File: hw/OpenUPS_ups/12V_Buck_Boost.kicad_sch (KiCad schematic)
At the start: 61 parts, among them Q601 AON7534, Q602 AON7534, Q603 AON7534, Q604 AON7534, U601 NCP81599

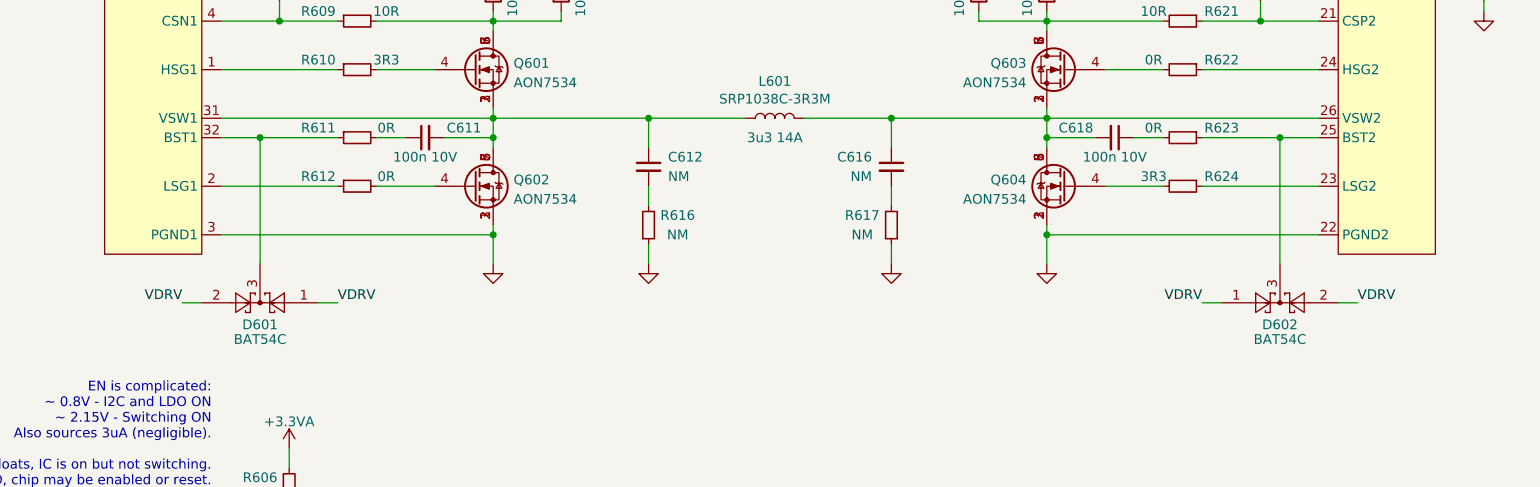
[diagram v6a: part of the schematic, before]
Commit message: Issue #23: Thin BAT54 diodes in converters
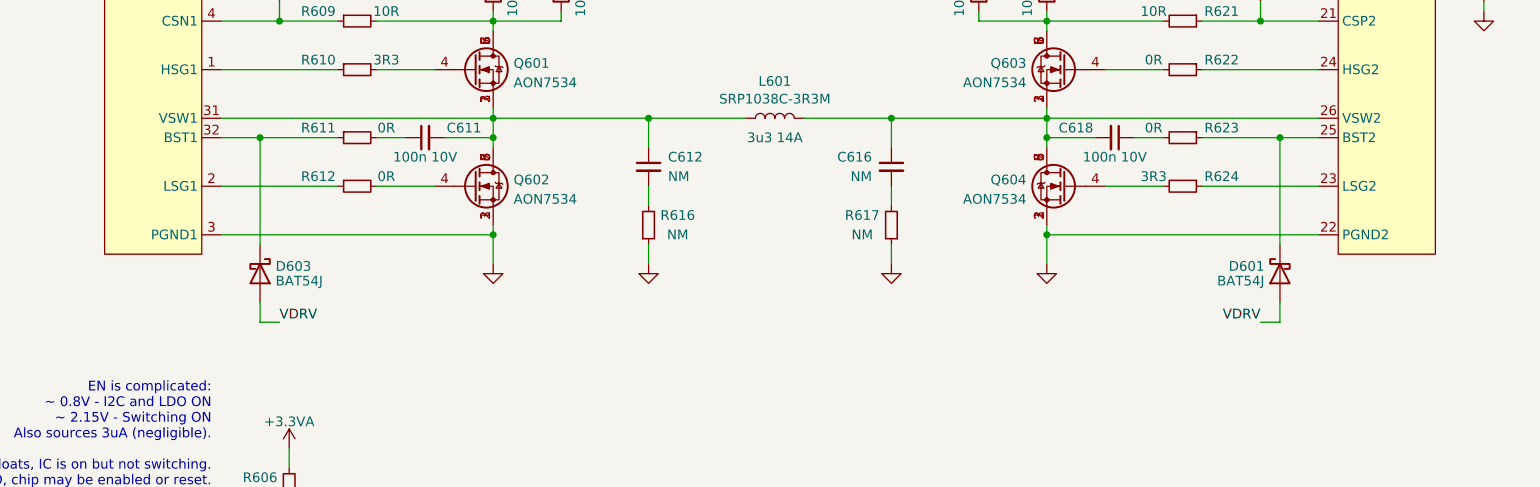
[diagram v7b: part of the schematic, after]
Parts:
- removed D601, D602: BAT54C, Package_TO_SOT_SMD:SOT-23, symbol Diode:BAT54C
- added D601, D603: BAT54J, Diode_SMD:D_SOD-323F, symbol Diode:BAT54J
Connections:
- net VDRV: now also D601.2 (A), D603.2 (A)
- net at R623.1, U601.25 (BST2): now also D601.1 (K)
- net at R611.1, U601.32 (BST1): now also D603.1 (K)
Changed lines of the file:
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@@
   (junction (at 110.49 165.1) (diameter 0) (color 0 0 0 0)
   )
-  (wire (pts (xy 99.06 110.49) (xy 101.6 110.49))
-    (stroke (width 0) (type default))
-  )
   (wire (pts (xy 247.65 63.5) (xy 240.03 63.5))
     (stroke (width 0) (type default))
@@
     (stroke (width 0) (type default))
   )
+  (wire (pts (xy 242.57 113.03) (xy 242.57 110.49))
+    (stroke (width 0) (type default))
+  )
   (wire (pts (xy 154.94 149.86) (xy 154.94 151.13))
     (stroke (width 0) (type default))
@@
     (stroke (width 0) (type default))
   )
-  (wire (pts (xy 116.84 110.49) (xy 119.38 110.49))
+  (wire (pts (xy 109.22 113.03) (xy 111.76 113.03))
     (stroke (width 0) (type default))
   )
@@
     (stroke (width 0) (type default))
   )
-  (wire (pts (xy 252.73 110.49) (xy 250.19 110.49))
-    (stroke (width 0) (type default))
-  )
   (wire (pts (xy 146.05 142.24) (xy 165.1 142.24))
     (stroke (width 0) (type default))
@@
     (stroke (width 0) (type default))
   )
-  (wire (pts (xy 242.57 88.9) (xy 242.57 105.41))
+  (wire (pts (xy 242.57 88.9) (xy 242.57 102.87))
     (stroke (width 0) (type default))
   )
@@
     (stroke (width 0) (type default))
   )
+  (wire (pts (xy 109.22 113.03) (xy 109.22 110.49))
+    (stroke (width 0) (type default))
+  )
   (wire (pts (xy 21.59 144.78) (xy 25.4 144.78))
     (stroke (width 0) (type default))
@@
     (stroke (width 0) (type default))
   )
+  (wire (pts (xy 242.57 113.03) (xy 240.03 113.03))
+    (stroke (width 0) (type default))
+  )
   (wire (pts (xy 104.14 88.9) (xy 109.22 88.9))
     (stroke (width 0) (type default))
@@
     (stroke (width 0) (type default))
   )
-  (wire (pts (xy 234.95 110.49) (xy 232.41 110.49))
-    (stroke (width 0) (type default))
-  )
   (wire (pts (xy 100.33 176.53) (xy 100.33 186.69))
     (stroke (width 0) (type default))
@@
     (stroke (width 0) (type default))
   )
-  (wire (pts (xy 109.22 88.9) (xy 109.22 105.41))
+  (wire (pts (xy 109.22 88.9) (xy 109.22 102.87))
     (stroke (width 0) (type default))
   )
@@
     (effects (font (size 1.27 1.27)) (justify left bottom))
   )
-  (label "VDRV" (at 156.21 139.7 0) (fields_autoplaced)
-    (effects (font (size 1.27 1.27)) (justify left bottom))
-  )
-  (label "VDRV" (at 232.41 110.49 180) (fields_autoplaced)
+  (label "VDRV" (at 240.03 113.03 180) (fields_autoplaced)
     (effects (font (size 1.27 1.27)) (justify right bottom))
   )
-  (label "VDRV" (at 252.73 110.49 0) (fields_autoplaced)
+  (label "VDRV" (at 156.21 139.7 0) (fields_autoplaced)
     (effects (font (size 1.27 1.27)) (justify left bottom))
   )
-  (label "VDRV" (at 119.38 110.49 0) (fields_autoplaced)
+  (label "VDRV" (at 111.76 113.03 0) (fields_autoplaced)
     (effects (font (size 1.27 1.27)) (justify left bottom))
   )
-  (label "VDRV" (at 99.06 110.49 180) (fields_autoplaced)
-    (effects (font (size 1.27 1.27)) (justify right bottom))
-  )
   (hierarchical_label "Vout" (shape output) (at 271.78 22.86 0) (fields_autoplaced)
     (effects (font (size 1.27 1.27)) (justify left))
@@
     )
   )
+  (symbol (lib_id "Diode:BAT54J") (at 242.57 106.68 90) (mirror x) (unit 1)
+    (in_bom yes) (on_board yes) (dnp no) (fields_autoplaced)
+    (property "Reference" "D601" (at 240.538 105.7188 90)
+      (effects (font (size 1.27 1.27)) (justify left))
+    )
+    (property "Value" "BAT54J" (at 240.538 107.6398 90)
+      (effects (font (size 1.27 1.27)) (justify left))
+    )
+    (property "Footprint" "Diode_SMD:D_SOD-323F" (at 247.015 106.68 0)
+      (effects (font (size 1.27 1.27)) hide)
+    )
+    (property "Datasheet" "https://assets.nexperia.com/documents/data-sheet/BAT54J.pdf" (at 242.57 106.68 0)
+      (effects (font (size 1.27 1.27)) hide)
+    )
+    (pin "1")
+    (pin "2")
+    (instances
+      (project "OpenUPS_ups"
+        (path "/f77faec3-eac4-47f3-a2de-ec4a039f4502/09fcd86a-cc7e-4bce-97cb-42a94055ba63"
+          (reference "D601") (unit 1)
+        )
+        (path "/f77faec3-eac4-47f3-a2de-ec4a039f4502/dfbaaed0-e564-4e21-900d-d5a65c0f1694"
+          (reference "D301") (unit 1)
+        )
+      )
+    )
+  )
   (symbol (lib_id "power:GND") (at 125.73 172.72 0) (unit 1)
     (in_bom yes) (on_board yes) (dnp no)
@@
     )
   )
-  (symbol (lib_id "Diode:BAT54C") (at 109.22 110.49 180) (unit 1)
-    (in_bom yes) (on_board yes) (dnp no) (fields_autoplaced)
-    (property "Reference" "D601" (at 109.22 113.3555 0)
-      (effects (font (size 1.27 1.27)))
-    )
-    (property "Value" "BAT54C" (at 109.22 115.2765 0)
-      (effects (font (size 1.27 1.27)))
-    )
-    (property "Footprint" "Package_TO_SOT_SMD:SOT-23" (at 107.315 113.665 0)
-      (effects (font (size 1.27 1.27)) (justify left) hide)
-    )
-    (property "Datasheet" "http://www.diodes.com/_files/datasheets/ds11005.pdf" (at 111.252 110.49 0)
-      (effects (font (size 1.27 1.27)) hide)
-    )
-    (pin "1")
-    (pin "2")
-    (pin "3")
-    (instances
-      (project "OpenUPS_ups"
-        (path "/f77faec3-eac4-47f3-a2de-ec4a039f4502/09fcd86a-cc7e-4bce-97cb-42a94055ba63"
-          (reference "D601") (unit 1)
-        )
-        (path "/f77faec3-eac4-47f3-a2de-ec4a039f4502/dfbaaed0-e564-4e21-900d-d5a65c0f1694"
-          (reference "D301") (unit 1)
-        )
-      )
-    )
-  )
   (symbol (lib_id "Device:R_Small") (at 269.24 58.42 0) (mirror x) (unit 1)
     (in_bom yes) (on_board yes) (dnp no)
@@
     )
   )
-  (symbol (lib_id "Diode:BAT54C") (at 242.57 110.49 0) (mirror x) (unit 1)
-    (in_bom yes) (on_board yes) (dnp no) (fields_autoplaced)
-    (property "Reference" "D602" (at 242.57 113.3555 0)
-      (effects (font (size 1.27 1.27)))
-    )
-    (property "Value" "BAT54C" (at 242.57 115.2765 0)
-      (effects (font (size 1.27 1.27)))
-    )
-    (property "Footprint" "Package_TO_SOT_SMD:SOT-23" (at 244.475 113.665 0)
-      (effects (font (size 1.27 1.27)) (justify left) hide)
-    )
-    (property "Datasheet" "http://www.diodes.com/_files/datasheets/ds11005.pdf" (at 240.538 110.49 0)
-      (effects (font (size 1.27 1.27)) hide)
-    )
-    (pin "1")
-    (pin "2")
-    (pin "3")
-    (instances
-      (project "OpenUPS_ups"
-        (path "/f77faec3-eac4-47f3-a2de-ec4a039f4502/09fcd86a-cc7e-4bce-97cb-42a94055ba63"
-          (reference "D602") (unit 1)
-        )
-        (path "/f77faec3-eac4-47f3-a2de-ec4a039f4502/dfbaaed0-e564-4e21-900d-d5a65c0f1694"
-          (reference "D302") (unit 1)
-        )
-      )
-    )
-  )
   (symbol (lib_id "power:GND") (at 240.03 54.61 0) (mirror x) (unit 1)
     (in_bom yes) (on_board yes) (dnp no)
@@
         )
       )
+    )
+  )
+  (symbol (lib_id "Diode:BAT54J") (at 109.22 106.68 270) (unit 1)
+    (in_bom yes) (on_board yes) (dnp no) (fields_autoplaced)
+    (property "Reference" "D603" (at 111.252 105.7188 90)
+      (effects (font (size 1.27 1.27)) (justify left))
+    )
+    (property "Value" "BAT54J" (at 111.252 107.6398 90)
+      (effects (font (size 1.27 1.27)) (justify left))
+    )
+    (property "Footprint" "Diode_SMD:D_SOD-323F" (at 104.775 106.68 0)
+      (effects (font (size 1.27 1.27)) hide)
+    )
+    (property "Datasheet" "https://assets.nexperia.com/documents/data-sheet/BAT54J.pdf" (at 109.22 106.68 0)
+      (effects (font (size 1.27 1.27)) hide)
+    )
+    (pin "1")
+    (pin "2")
+    (instances
+      (project "OpenUPS_ups"
+        (path "/f77faec3-eac4-47f3-a2de-ec4a039f4502/09fcd86a-cc7e-4bce-97cb-42a94055ba63"
+          (reference "D603") (unit 1)
+        )
+        (path "/f77faec3-eac4-47f3-a2de-ec4a039f4502/dfbaaed0-e564-4e21-900d-d5a65c0f1694"
+          (reference "D303") (unit 1)
+        )
+      )

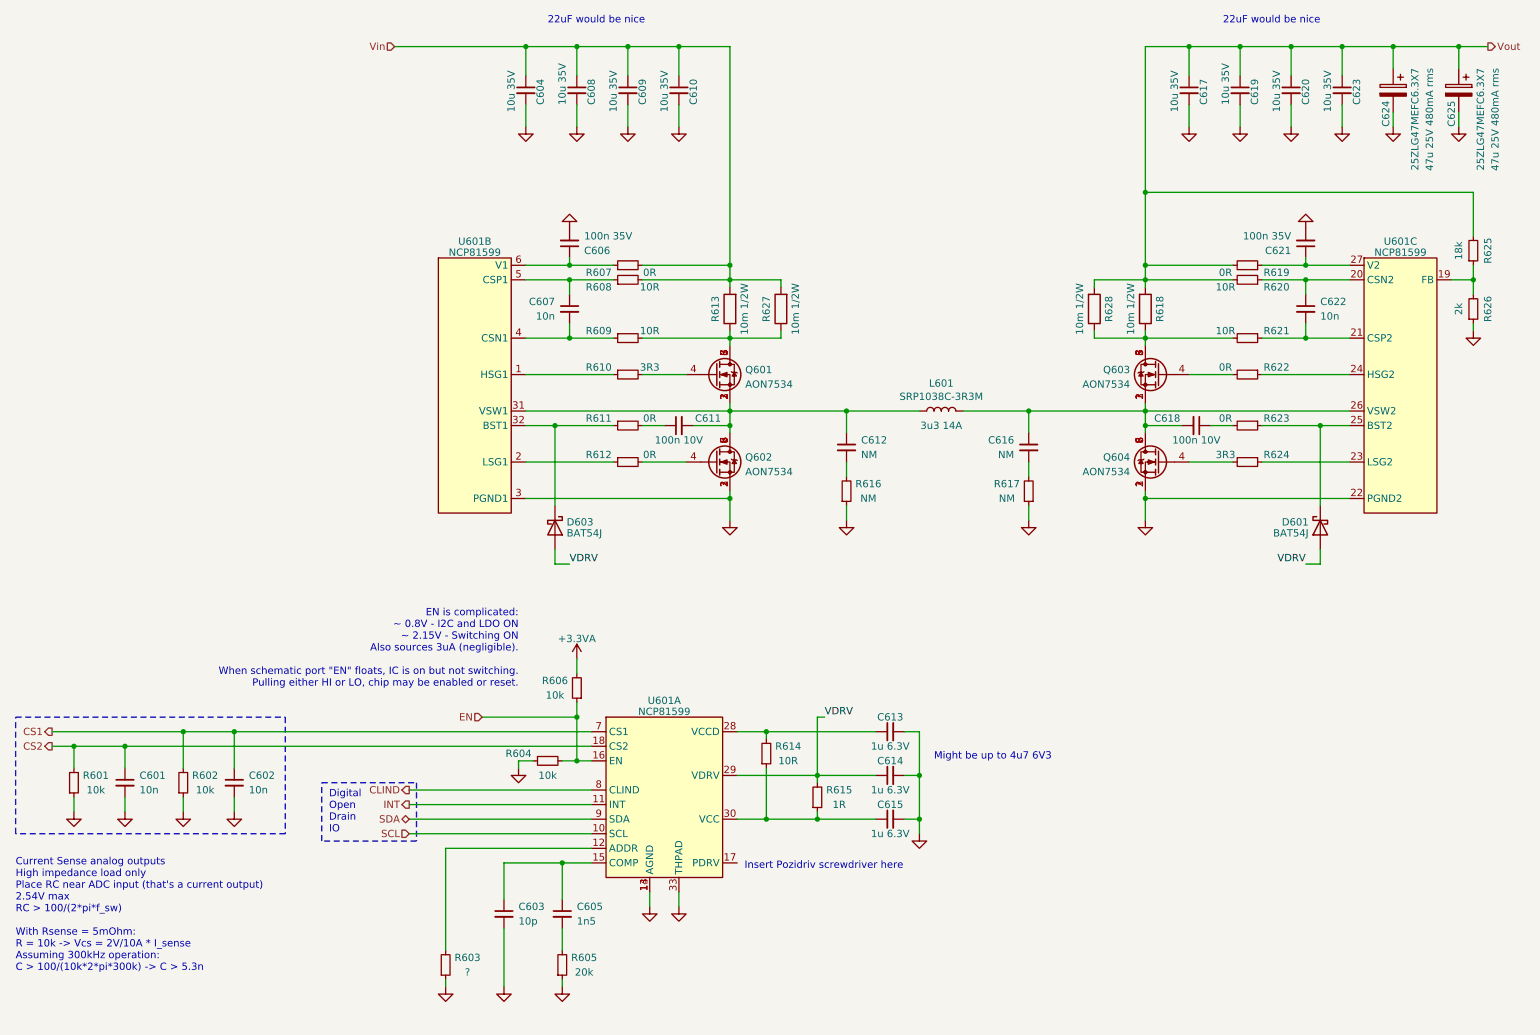
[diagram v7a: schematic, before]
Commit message: 12V converter layout
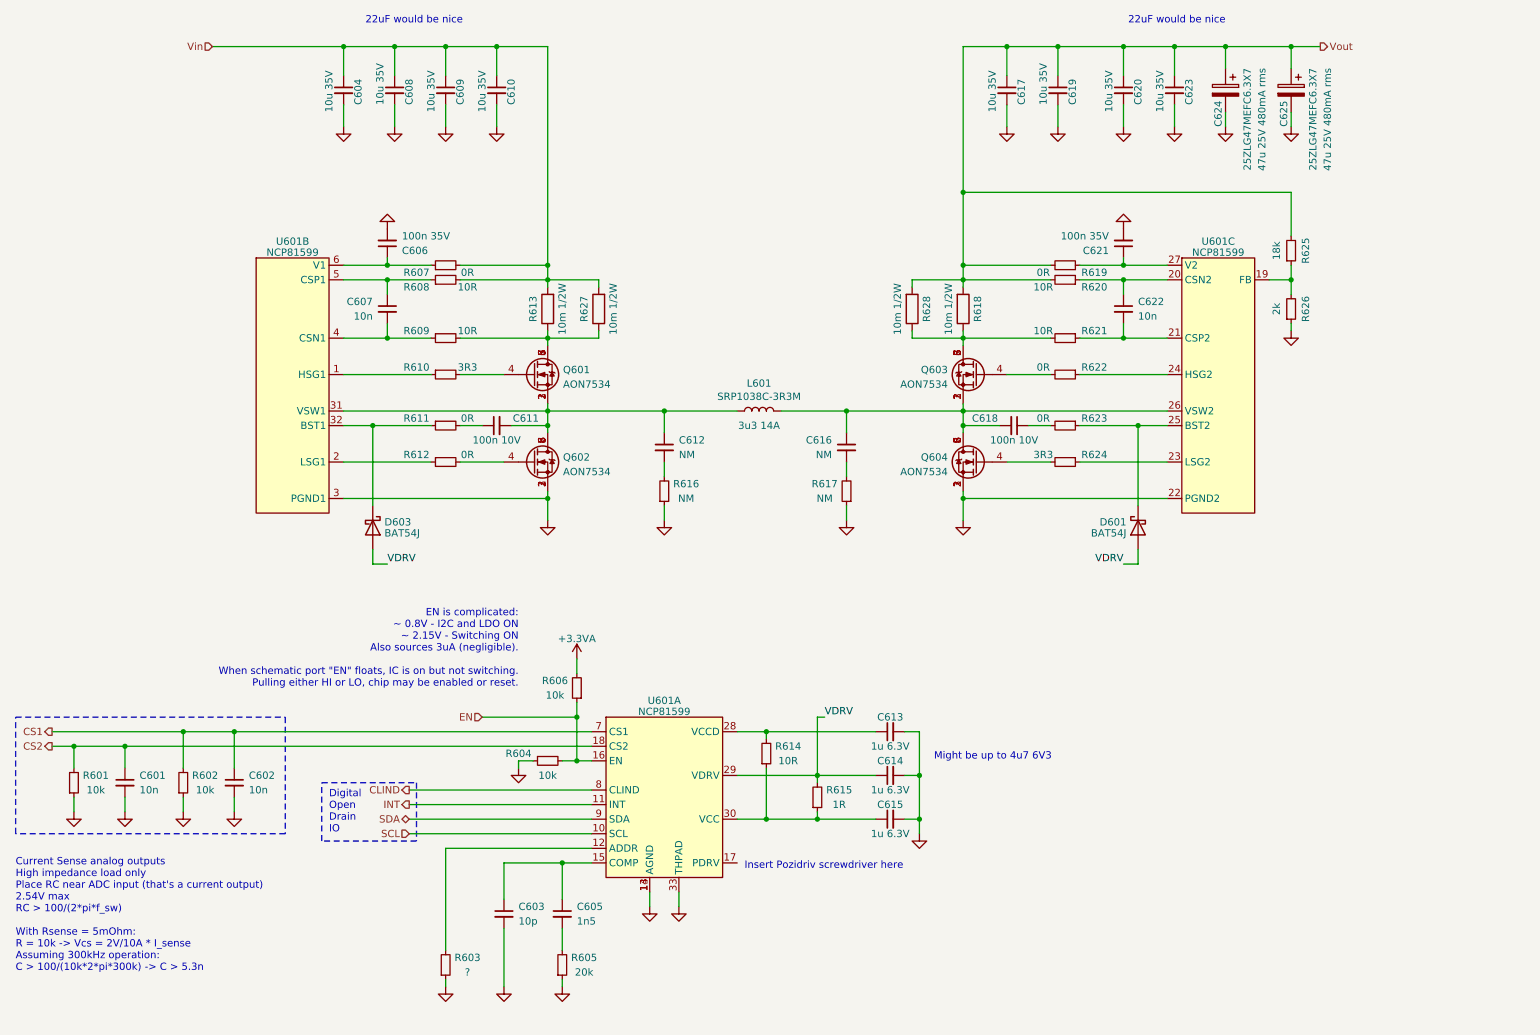
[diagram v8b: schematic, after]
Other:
- moved on the sheet: C604, C606, C607, C608, C609, C610, C611, C612, C616, C617, C618, C619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
